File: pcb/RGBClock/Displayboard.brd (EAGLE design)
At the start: 100 x 80 mm, 66 parts, among them IC1 MCP23017SO, U1 LP3878MR-ADJ, U2 P82B96DR, U3 P82B96DR, U4 PCA9685PW, U5 TPS71533DCKR, U6 ZXLD1362ET5TA, U7 74HCT1G14GW, U8 74HCT1G86GW, X2 43045-0400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

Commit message: Cleanup schematic
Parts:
- R10: value A0-1 -> A0-0
- R11: value A0-0 -> A1-1
- R12: value A1-1 -> A1-0
- R13: value A1-0 -> A0-1
- R14: value A2-1 -> A0-0
- R15: value A2-0 -> 0.833R; device resistor:R0402 -> resistor:R0603
- R16: value A1-1 -> A0-1
- R17: value A1-1 -> A0-0
- R18, R7: value A0-1 -> A1-1
- R19, R8: value A0-0 -> A1-0
- R20, R5: value A1-1 -> A2-1
- R21: value A2-1 -> A2-0
- R22: value A1-0 -> 3300; device resistor:R0402 -> rcl:0204/7
- R23: value A2-0 -> A1-1
- R24: value 3300 -> A1-1; device rcl:0204/7 -> resistor:R0402
- R6: value A1-0 -> A2-0
- R9: value 0.833R -> A0-1; device resistor:R0603 -> resistor:R0402
- moved R24 102.2 mm to (88.9, 38.1)
- moved R22 58.7 mm to (-2.54, -7.62)
- moved R23 50.6 mm to (88.9, 39.4)
- moved R19 50.3 mm to (88.9, 22.9), turned to 180 degrees
- moved R21 49.9 mm to (88.9, 24.1), turned to 180 degrees
- moved R10 46.8 mm to (39.4, 31.8), turned to 0 degrees
- moved R18 42.8 mm to (85.1, 22.9), turned to 180 degrees
- moved R20 42.4 mm to (85.1, 24.1), turned to 180 degrees
- moved R15 35.3 mm to (58.4, 41.9)
- moved R5 32.9 mm to (39.4, 30.5)
- moved R6 29.0 mm to (39.4, 29.2)
- moved R7 28.4 mm to (43.2, 30.5)
- moved R8 24.4 mm to (43.2, 29.2)
- moved R12 21.7 mm to (64.8, 15.2), turned to 0 degrees
- moved R11 21.3 mm to (68.6, 15.2), turned to 0 degrees
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- renumbered X7 to X1
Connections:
- net +5V: now also R11.2, R13.2, R16.2, R9.2; no longer R10.2, R12.2, R14.2, R21.2
- net GND: now also C16.2, C18.1, R10.1, R12.1, R14.1, R17.1, R21.1; no longer C16.1, C18.2, R11.1, R13.1, R15.1, R22.1, R23.1
- net N$1: now also R15.1; no longer R9.1
- net N$18: now also R18.1, R19.2; no longer R12.1, R13.2
- net N$19: now also R16.1, R17.2; no longer R10.1, R11.2
- net N$20: now also R5.1, R6.2; no longer R21.1, R23.2
- net N$21: now also R20.1, R21.2; no longer R14.1, R15.2
- net N$23: now also C18.2; no longer C16.2
- net N$27: now also R24.1; no longer R17.1
- net N$28: now also R23.1; no longer R16.1
- net N$29: now also R7.1, R8.2; no longer R20.1, R22.2
- net N$3: now also R22.2; no longer R24.2
- net N$30: now also R22.1; no longer R24.1
- net N$4: now also C16.1; no longer C18.1
- net N$41: now also R13.1, R14.2; no longer R7.1, R8.2
- net N$42: now also R11.1, R12.2; no longer R5.1, R6.2
- net N$43: now also R10.2, R9.1; no longer R18.1, R19.2
- net SCL: now also R23.2; no longer R16.2
- net SDA: now also R24.2; no longer R17.2
- net VCC: now also R15.2; no longer R9.2

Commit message: 
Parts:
- R22: value 3300 -> 1k
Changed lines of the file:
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@@
 <attribute name="OC_FARNELL" value="1085266" x="63.5" y="36.83" size="1.778" layer="27" rot="R180" display="off"/>
 </element>
-<element name="R22" library="rcl" package="0204/7" value="3300" x="-2.54" y="-7.62"/>
+<element name="R22" library="rcl" package="0204/7" value="1k" x="-2.54" y="-7.62"/>
 <element name="C19" library="rcl" package="C0805" value="22n" x="-5.08" y="-12.7"/>
 </elements>

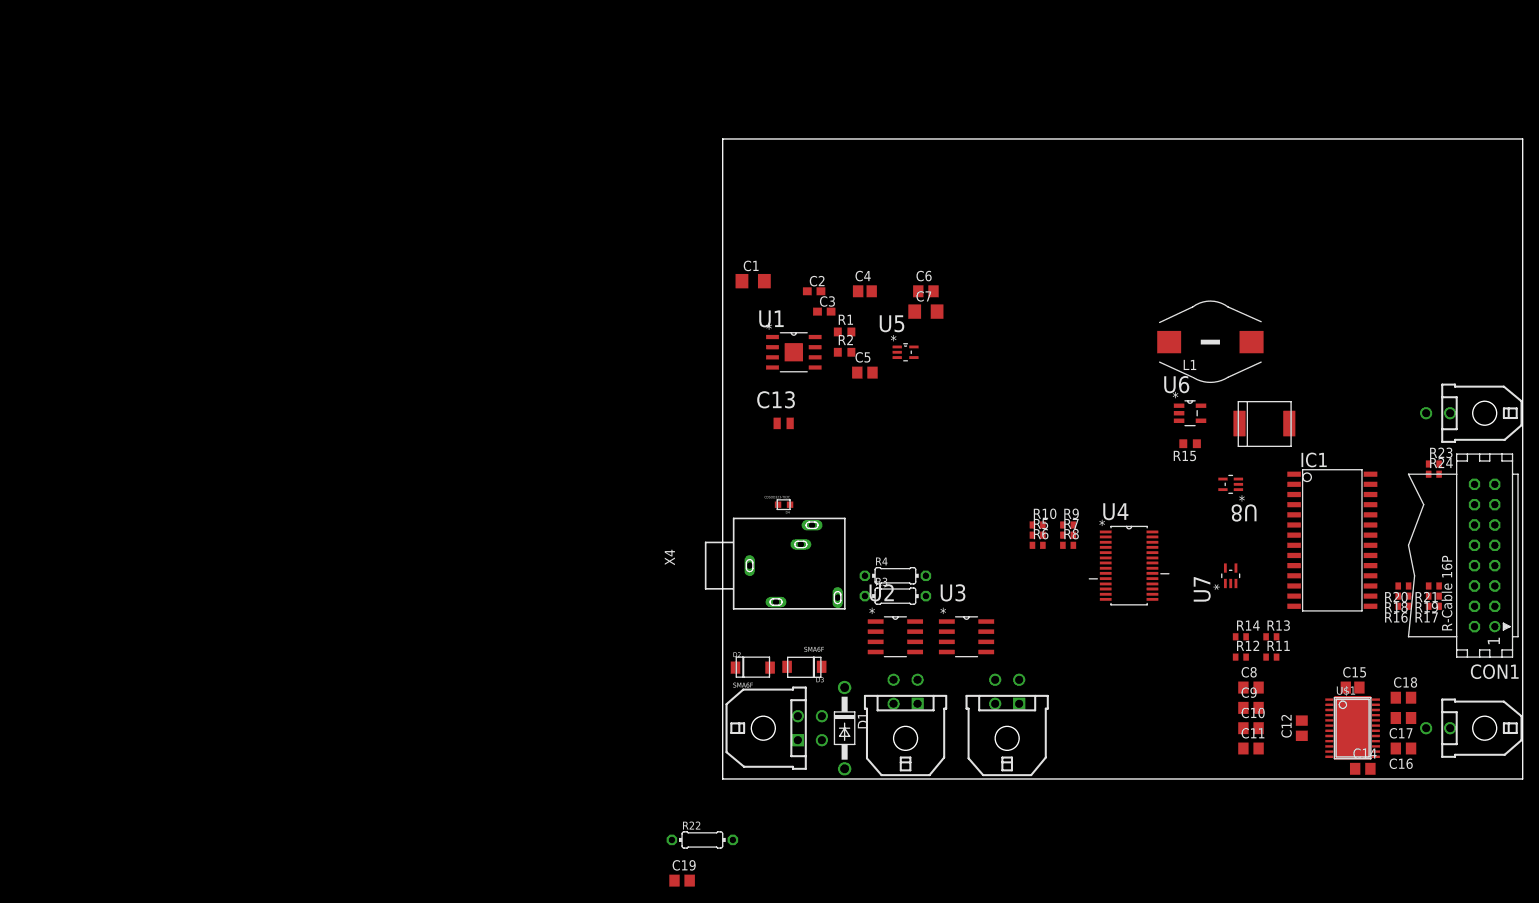
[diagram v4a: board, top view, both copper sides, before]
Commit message: Routing displayoard and cleanup board
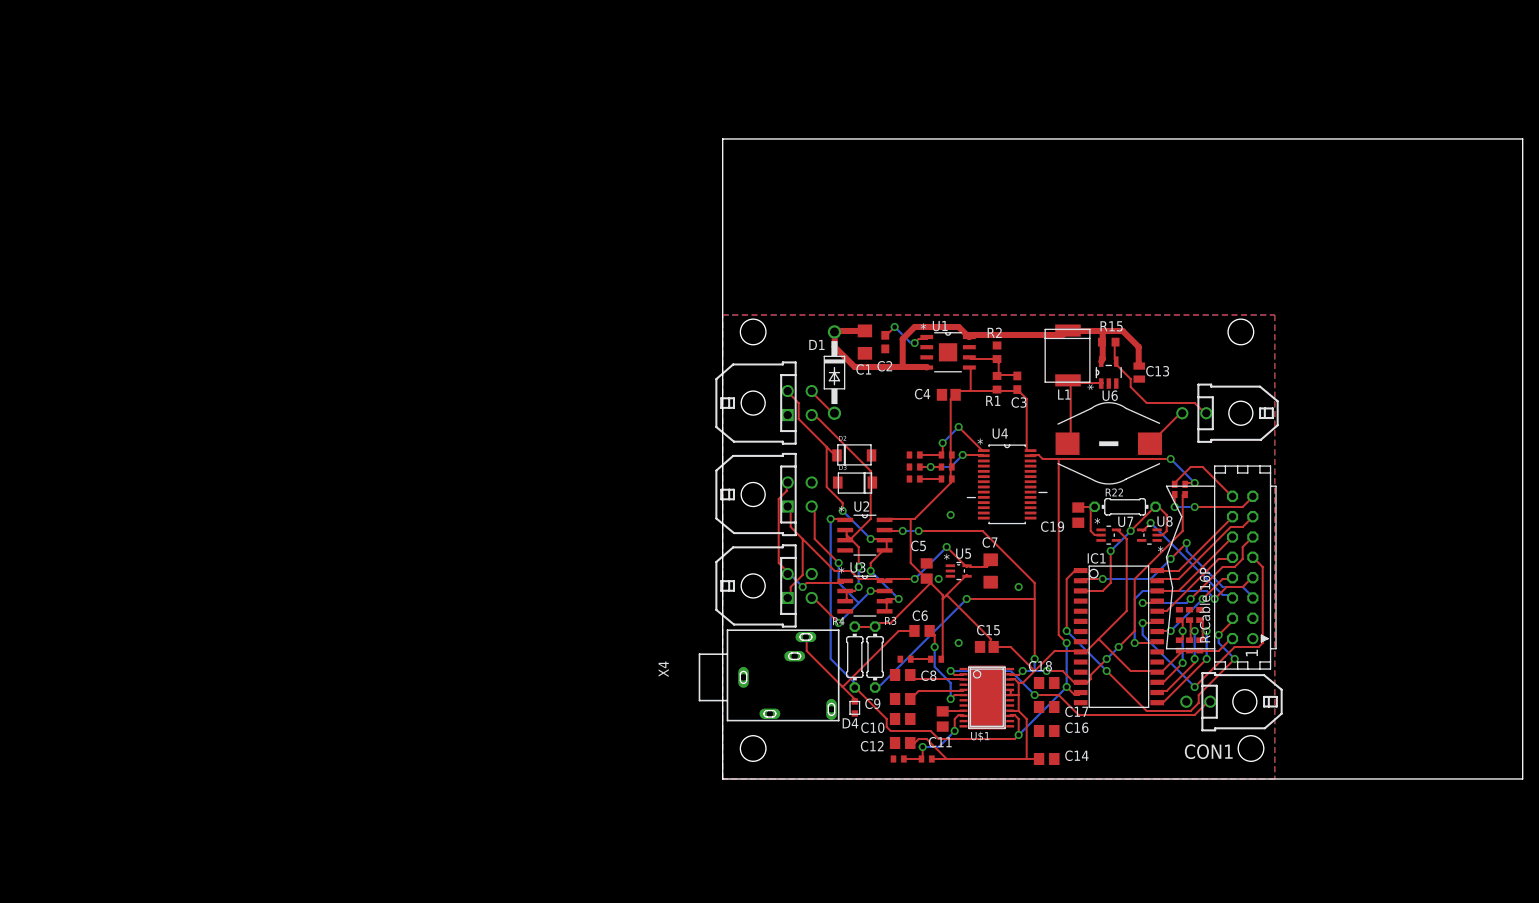
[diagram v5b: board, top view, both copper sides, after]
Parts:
- R23: value A1-1 -> SCL
- R24: value A1-1 -> SDA
- moved C19 67.4 mm to (44.5, 33.0), turned to 90 degrees
- moved R22 67.3 mm to (50.3, 34.0)
- moved C12 49.9 mm to (22.5, 4.50), turned to 180 degrees
- moved C15 46.0 mm to (33.0, 16.5), turned to 180 degrees
- moved U$1 45.9 mm to (33.0, 10.2)
- moved R11 44.9 mm to (25.5, 2.50)
- moved C13 44.9 mm to (52.1, 50.8), turned to 90 degrees
- moved C16 44.6 mm to (40.5, 6.00), turned to 0 degrees
- moved C18 44.6 mm to (40.5, 12.0), turned to 180 degrees
- moved R12 44.6 mm to (22.0, 2.50)
- moved C17 44.6 mm to (40.5, 9.00), turned to 0 degrees
- moved D1 44.5 mm to (14.0, 50.8)
- moved C8 43.6 mm to (22.5, 13.0)
- moved C10 43.6 mm to (22.5, 7.50)
- moved C9 43.6 mm to (22.5, 10.0)
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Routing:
- net +5V: track 0.00 -> 175.3 mm
- net SDA: track 0.00 -> 115.1 mm, vias 0 -> 6
- net SCL: track 0.00 -> 96.2 mm, vias 0 -> 8
- net VCC: track 0.00 -> 60.0 mm
- net RS: track 0.00 -> 44.0 mm, vias 0 -> 4
- net +3V3: track 0.00 -> 42.3 mm, vias 0 -> 2
- net N$22: track 0.00 -> 40.1 mm, vias 0 -> 4
- net N$12: track 0.00 -> 37.2 mm, vias 0 -> 2
- net D2: track 0.00 -> 34.6 mm, vias 0 -> 2
- net N$2: track 0.00 -> 32.5 mm, vias 0 -> 2
- net RW: track 0.00 -> 26.9 mm, vias 0 -> 3
- net N$9: track 0.00 -> 26.7 mm, vias 0 -> 3
- net D0: track 0.00 -> 25.0 mm, vias 0 -> 2
- net N$49: track 0.00 -> 22.4 mm
- net N$3: track 0.00 -> 21.3 mm, vias 0 -> 2
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- added copper zone on layer 1, net GND
- added copper zone on layer 16, net GND

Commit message: Panelizing to a big board ...
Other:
- board size 100 x 80 mm -> 69 x 58.5 mm
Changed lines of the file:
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@@
 <board>
 <plain>
-<wire x1="0" y1="0" x2="100" y2="0" width="0" layer="20"/>
-<wire x1="100" y1="0" x2="100" y2="80" width="0" layer="20"/>
-<wire x1="100" y1="80" x2="0" y2="80" width="0" layer="20"/>
-<wire x1="0" y1="80" x2="0" y2="0" width="0" layer="20"/>
+<wire x1="0" y1="0" x2="69" y2="0" width="0" layer="20"/>
+<wire x1="69" y1="0" x2="69" y2="58.5" width="0" layer="20"/>
+<wire x1="69" y1="58.5" x2="0" y2="58.5" width="0" layer="20"/>
+<wire x1="0" y1="58.5" x2="0" y2="0" width="0" layer="20"/>
 <hole x="3.81" y="3.81" drill="3.2"/>
 <hole x="66.04" y="3.81" drill="3.2"/>

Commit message: Beta version master pcb (not complete routed !)
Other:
- board size 69 x 58.5 mm -> 70 x 58.5 mm
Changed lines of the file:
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@@
 <board>
 <plain>
-<wire x1="0" y1="0" x2="69" y2="0" width="0" layer="20"/>
-<wire x1="69" y1="0" x2="69" y2="58.5" width="0" layer="20"/>
-<wire x1="69" y1="58.5" x2="0" y2="58.5" width="0" layer="20"/>
+<wire x1="0" y1="0" x2="70" y2="0" width="0" layer="20"/>
+<wire x1="70" y1="0" x2="70" y2="58.5" width="0" layer="20"/>
+<wire x1="70" y1="58.5" x2="0" y2="58.5" width="0" layer="20"/>
 <wire x1="0" y1="58.5" x2="0" y2="0" width="0" layer="20"/>
 <hole x="3.81" y="3.81" drill="3.2"/>
@@
 <contactref element="U8" pad="3"/>
 <contactref element="C19" pad="1"/>
-<polygon width="0.4064" layer="1">
-<vertex x="0" y="58"/>
-<vertex x="69" y="58"/>
-<vertex x="69" y="0"/>
-<vertex x="0" y="0"/>
-</polygon>
-<polygon width="0.4064" layer="16">
-<vertex x="0" y="58"/>
-<vertex x="69" y="58"/>
-<vertex x="69" y="0"/>
-<vertex x="0" y="0"/>
-</polygon>
 <via x="37" y="24" extent="1-16" drill="0.6" shape="square"/>
 <via x="29.5" y="17" extent="1-16" drill="0.6" shape="square"/>
 <via x="27" y="25" extent="1-16" drill="0.6" shape="square"/>
 <via x="28.5" y="33" extent="1-16" drill="0.6" shape="square"/>
+<polygon width="0.8128" layer="1">
+<vertex x="0" y="58.5"/>
+<vertex x="70" y="58.5"/>
+<vertex x="70" y="0"/>
+<vertex x="0" y="0"/>
+</polygon>
+<polygon width="0.8128" layer="16">
+<vertex x="0" y="58.5"/>
+<vertex x="70" y="58.5"/>
+<vertex x="70" y="0"/>
+<vertex x="0" y="0"/>
+</polygon>
 <wire x1="47.2948" y1="29.8196" x2="54.3052" y2="31.1404" width="0" layer="19" extent="1-1"/>
-<wire x1="25.503" y1="52.705" x2="28.17" y2="53.34" width="0" layer="19" extent="1-1"/>
 <wire x1="41.45" y1="12" x2="41.45" y2="9" width="0" layer="19" extent="1-1"/>
-<wire x1="21.55" y1="7.5" x2="21.55" y2="4.5" width="0" layer="19" extent="1-1"/>
-<wire x1="30.1022" y1="7.235" x2="27.5" y2="6.55" width="0" layer="19" extent="1-1"/>
-<wire x1="14.39" y1="37.05" x2="11.13" y2="37.06" width="0" layer="19" extent="1-1"/>
 <wire x1="48.26" y1="49.4284" x2="52.07" y2="49.9872" width="0" layer="19" extent="1-1"/>
 <wire x1="44.75" y1="14.62" x2="41.45" y2="12" width="0" layer="19" extent="1-1"/>
+<wire x1="35.9378" y1="6.585" x2="41.45" y2="6" width="0" layer="19" extent="1-1"/>
+<wire x1="33.04" y1="10.18" x2="35.9378" y2="6.585" width="0" layer="19" extent="1-1"/>
+<wire x1="28.4586" y1="26" x2="27" y2="25" width="0" layer="19" extent="1-1"/>
+<wire x1="25.503" y1="52.705" x2="28.17" y2="53.34" width="0" layer="19" extent="1-1"/>
+<wire x1="21.55" y1="7.5" x2="21.55" y2="4.5" width="0" layer="19" extent="1-1"/>
+<wire x1="14.39" y1="37.05" x2="11.13" y2="37.06" width="0" layer="19" extent="1-1"/>
+<wire x1="30.1022" y1="13.735" x2="29.5" y2="17" width="0" layer="19" extent="1-1"/>
+<wire x1="30.1022" y1="7.235" x2="33.04" y2="10.18" width="0" layer="19" extent="1-1"/>
+<wire x1="27.5" y1="6.55" x2="30.1022" y2="7.235" width="0" layer="19" extent="1-1"/>
+<wire x1="15.3162" y1="28.575" x2="11.13" y2="25.63" width="0" layer="19" extent="1-1"/>
+<wire x1="20.32" y1="53.76" x2="25.503" y2="52.705" width="0" layer="19" extent="1-1"/>
+<wire x1="17.78" y1="53.21" x2="20.32" y2="53.76" width="0" layer="19" extent="1-1"/>
+<wire x1="32.639" y1="38.4556" x2="32.639" y2="32.6136" width="0" layer="19" extent="1-1"/>
+<wire x1="38.481" y1="39.116" x2="32.639" y2="39.116" width="0" layer="19" extent="1-1"/>
+<wire x1="15.3162" y1="20.955" x2="11.13" y2="25.63" width="0" layer="19" extent="1-1"/>
+<wire x1="59.63" y1="21.16" x2="66.27" y2="17.55" width="0" layer="19" extent="1-1"/>
 </signal>
 <signal name="VCC" class="2">
